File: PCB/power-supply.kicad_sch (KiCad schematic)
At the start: 18 parts, among them J2 DF63-5P-3.96DSA

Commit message: preliminary routing completed
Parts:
- removed DBG1, DBG2, DBG3, DBG4, DBG5, DBG6: ~, Oro Footprints:DebugPin, symbol Oro:DebugPin
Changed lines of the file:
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@@
   (junction (at 187.96 98.425) (diameter 0) (color 0 0 0 0)
-  )
-  (junction (at 195.58 100.965) (diameter 0) (color 0 0 0 0)
-  )
-  (junction (at 264.16 98.425) (diameter 0) (color 0 0 0 0)
   )
   (junction (at 218.44 118.745) (diameter 0) (color 0 0 0 0)
@@
     (property "Netclass" "5V" (at 144.145 92.71 0)
       (effects (font (size 1.27 1.27) italic) (justify left))
-    )
-  )
-  (symbol (lib_id "Oro:DebugPin") (at 59.055 100.33 180) (unit 1)
-    (in_bom no) (on_board yes) (dnp no)
-    (property "Reference" "DBG2" (at 53.34 100.33 0)
-      (effects (font (size 1.27 1.27)) hide)
-    )
-    (property "Value" "~" (at 59.055 100.33 0)
-      (effects (font (size 1.27 1.27)) hide)
-    )
-    (property "Footprint" "Oro Footprints:DebugPin" (at 57.785 102.87 0)
-      (effects (font (size 1.27 1.27)) hide)
-    )
-    (property "Datasheet" "" (at 59.055 100.33 0)
-      (effects (font (size 1.27 1.27)) hide)
-    )
-    (property "Sim.Enable" "0" (at 45.085 102.87 0)
-      (effects (font (size 1.27 1.27)) hide)
-    )
-    (pin "1")
-    (instances
-      (project "OroLink"
-        (path "/e89dcd22-1250-4a5b-b778-1c95a0dd623d/f955395e-bf1a-4ef3-9cfe-ec9d49f66988"
-          (reference "DBG2") (unit 1)
-        )
-      )
     )
   )
@@
     )
   )
-  (symbol (lib_id "Oro:DebugPin") (at 59.055 102.87 180) (unit 1)
-    (in_bom no) (on_board yes) (dnp no)
-    (property "Reference" "DBG3" (at 53.34 102.87 0)
-      (effects (font (size 1.27 1.27)) hide)
-    )
-    (property "Value" "~" (at 59.055 102.87 0)
-      (effects (font (size 1.27 1.27)) hide)
-    )
-    (property "Footprint" "Oro Footprints:DebugPin" (at 57.785 105.41 0)
-      (effects (font (size 1.27 1.27)) hide)
-    )
-    (property "Datasheet" "" (at 59.055 102.87 0)
-      (effects (font (size 1.27 1.27)) hide)
-    )
-    (property "Sim.Enable" "0" (at 45.085 105.41 0)
-      (effects (font (size 1.27 1.27)) hide)
-    )
-    (pin "1")
-    (instances
-      (project "OroLink"
-        (path "/e89dcd22-1250-4a5b-b778-1c95a0dd623d/f955395e-bf1a-4ef3-9cfe-ec9d49f66988"
-          (reference "DBG3") (unit 1)
-        )
-      )
-    )
-  )
   (symbol (lib_id "SamacSys_Parts:CSD13380F3T") (at 125.095 112.395 90) (mirror x) (unit 1)
     (in_bom yes) (on_board yes) (dnp no) (fields_autoplaced)
@@
         (path "/e89dcd22-1250-4a5b-b778-1c95a0dd623d/f955395e-bf1a-4ef3-9cfe-ec9d49f66988"
           (reference "R8") (unit 1)
-        )
-      )
-    )
-  )
-  (symbol (lib_id "Oro:DebugPin") (at 264.16 98.425 0) (unit 1)
-    (in_bom no) (on_board yes) (dnp no)
-    (property "Reference" "DBG6" (at 269.875 98.425 0)
-      (effects (font (size 1.27 1.27)) hide)
-    )
-    (property "Value" "~" (at 264.16 98.425 0)
-      (effects (font (size 1.27 1.27)) hide)
-    )
-    (property "Footprint" "Oro Footprints:DebugPin" (at 265.43 95.885 0)
-      (effects (font (size 1.27 1.27)) hide)
-    )
-    (property "Datasheet" "" (at 264.16 98.425 0)
-      (effects (font (size 1.27 1.27)) hide)
-    )
-    (property "Sim.Enable" "0" (at 278.13 95.885 0)
-      (effects (font (size 1.27 1.27)) hide)
-    )
-    (pin "1")
-    (instances
-      (project "OroLink"
-        (path "/e89dcd22-1250-4a5b-b778-1c95a0dd623d/f955395e-bf1a-4ef3-9cfe-ec9d49f66988"
-          (reference "DBG6") (unit 1)
         )
       )
@@
     )
   )
-  (symbol (lib_id "Oro:DebugPin") (at 59.055 105.41 180) (unit 1)
-    (in_bom no) (on_board yes) (dnp no)
-    (property "Reference" "DBG4" (at 53.34 105.41 0)
-      (effects (font (size 1.27 1.27)) hide)
-    )
-    (property "Value" "~" (at 59.055 105.41 0)
-      (effects (font (size 1.27 1.27)) hide)
-    )
-    (property "Footprint" "Oro Footprints:DebugPin" (at 57.785 107.95 0)
-      (effects (font (size 1.27 1.27)) hide)
-    )
-    (property "Datasheet" "" (at 59.055 105.41 0)
-      (effects (font (size 1.27 1.27)) hide)
-    )
-    (property "Sim.Enable" "0" (at 45.085 107.95 0)
-      (effects (font (size 1.27 1.27)) hide)
-    )
-    (pin "1")
-    (instances
-      (project "OroLink"
-        (path "/e89dcd22-1250-4a5b-b778-1c95a0dd623d/f955395e-bf1a-4ef3-9cfe-ec9d49f66988"
-          (reference "DBG4") (unit 1)
-        )
-      )
-    )
-  )
   (symbol (lib_id "Oro:BOM Part") (at 53.34 120.015 0) (unit 1)
     (in_bom yes) (on_board no) (dnp no)
@@
         )
       )
-    )
-  )
-  (symbol (lib_id "Oro:DebugPin") (at 195.58 100.965 180) (unit 1)
-    (in_bom no) (on_board yes) (dnp no)
-    (property "Reference" "DBG5" (at 189.865 100.965 0)
-      (effects (font (size 1.27 1.27)) hide)
-    )
-    (property "Value" "~" (at 195.58 100.965 0)
-      (effects (font (size 1.27 1.27)) hide)
-    )
-    (property "Footprint" "Oro Footprints:DebugPin" (at 194.31 103.505 0)
-      (effects (font (size 1.27 1.27)) hide)
-    )
-    (property "Datasheet" "" (at 195.58 100.965 0)
-      (effects (font (size 1.27 1.27)) hide)
-    )
-    (property "Sim.Enable" "0" (at 181.61 103.505 0)
-      (effects (font (size 1.27 1.27)) hide)
-    )
-    (pin "1")
-    (instances
-      (project "OroLink"
-        (path "/e89dcd22-1250-4a5b-b778-1c95a0dd623d/f955395e-bf1a-4ef3-9cfe-ec9d49f66988"
-          (reference "DBG5") (unit 1)
-        )
-      )
-    )
-  )
-  (symbol (lib_id "Oro:DebugPin") (at 59.055 97.79 180) (unit 1)
-    (in_bom no) (on_board yes) (dnp no)
-    (property "Reference" "DBG1" (at 53.34 97.79 0)
-      (effects (font (size 1.27 1.27)) hide)
-    )
-    (property "Value" "~" (at 59.055 97.79 0)
-      (effects (font (size 1.27 1.27)) hide)
-    )
-    (property "Footprint" "Oro Footprints:DebugPin" (at 57.785 100.33 0)
-      (effects (font (size 1.27 1.27)) hide)
-    )
-    (property "Datasheet" "" (at 59.055 97.79 0)
-      (effects (font (size 1.27 1.27)) hide)
-    )
-    (property "Sim.Enable" "0" (at 45.085 100.33 0)
-      (effects (font (size 1.27 1.27)) hide)
-    )
-    (pin "1")
-    (instances
-      (project "OroLink"
-        (path "/e89dcd22-1250-4a5b-b778-1c95a0dd623d/f955395e-bf1a-4ef3-9cfe-ec9d49f66988"
-          (reference "DBG1") (unit 1)
-        )
-      )

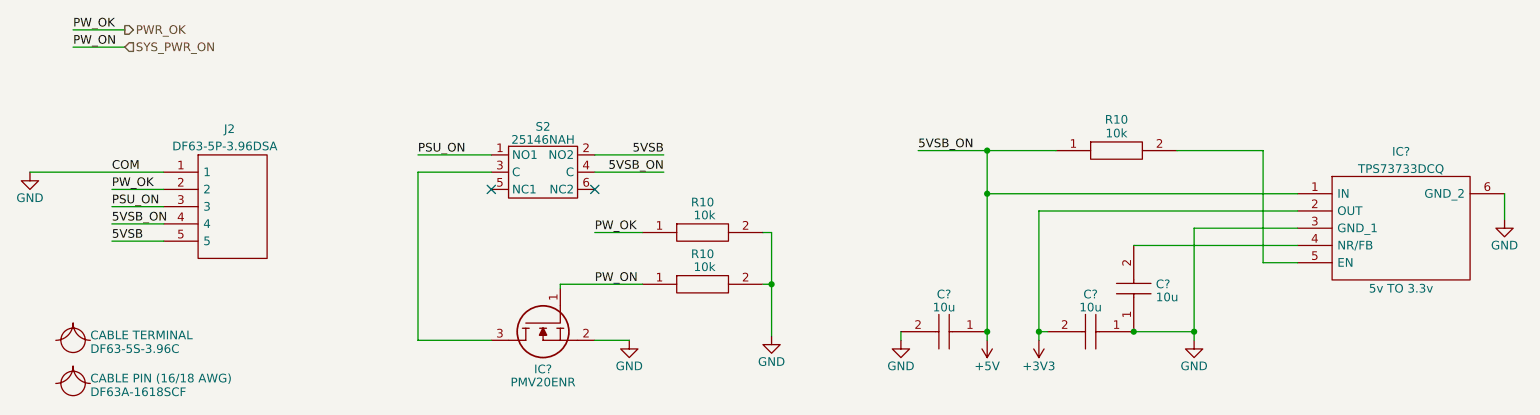
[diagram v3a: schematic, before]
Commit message: eliminate power switch in lieu of direct power + sys s.b. mosfet (closes #38)
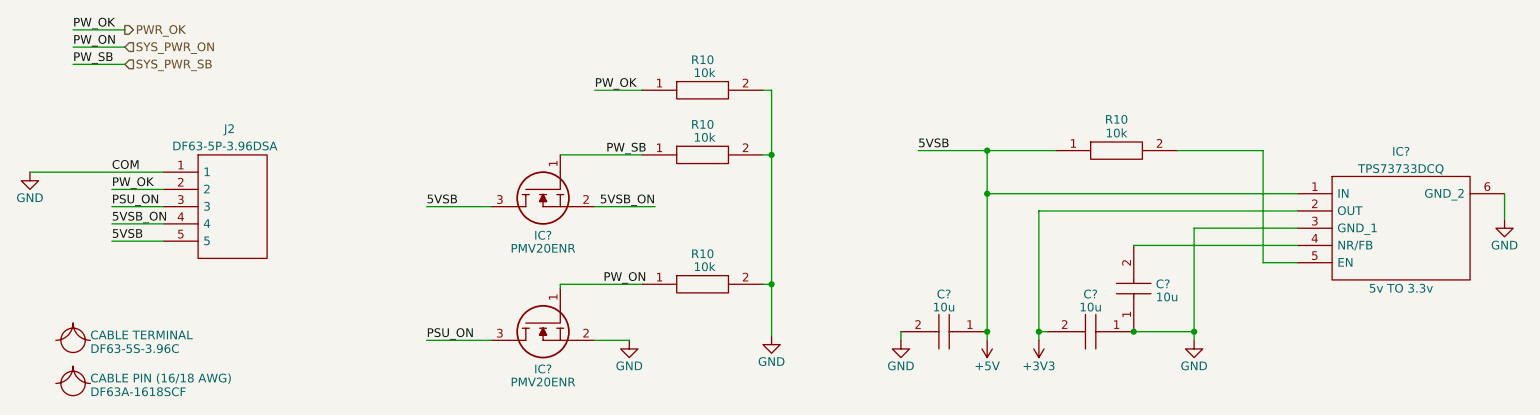
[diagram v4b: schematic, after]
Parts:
- removed S2: 25146NAH, Oro Footprints:25146NAH, symbol Oro:25146NAH
- added IC?: PMV20ENR, SamacSys_Parts:SOT95P230X110-3N, symbol SamacSys_Parts:CSD13380F3T
- added R10: 10k, RESC1005X40N, symbol SamacSys_Parts:RK73H1ETTP1002F
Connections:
- net 5VSB is gone; now on net +5V: J2.5
- net +5V: now also IC?.3; no longer J2.4
- net GND: now also R10.2
- net PSU_ON: now also IC?.3
- new net: IC?.1, R10.1
- new net 5VSB_ON: IC?.2, J2.4
- no-connect marks 2 -> 0
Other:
- moved on the sheet: R10

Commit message: switch out linear regular for one with larger max current (closes #43)
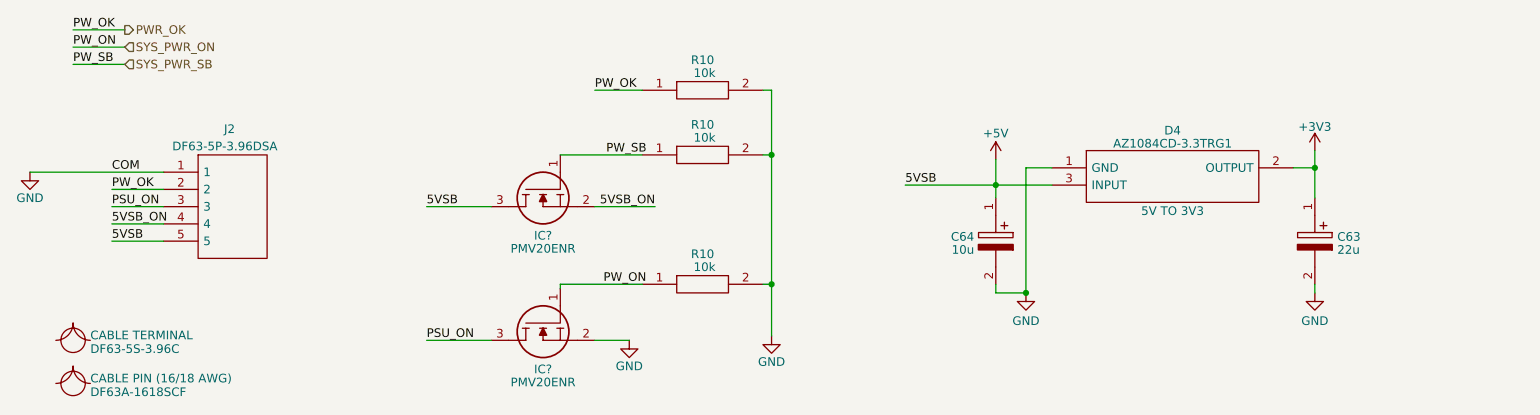
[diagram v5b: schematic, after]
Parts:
- removed C? (x3): 10u, SamacSys_Parts:CAPC2012X135N, symbol SamacSys_Parts:LMK212ABJ106KG8T
- removed IC?: TPS73733DCQ, SamacSys_Parts:SOT127P706X180-6N, symbol SamacSys_Parts:TPS73733DCQR
- removed R10: 10k, RESC1005X40N, symbol SamacSys_Parts:RK73H1ETTP1002F
- added C63: 22u, CAPAE660X800N, symbol SamacSys_Parts:UCZ1H220MCL1GS
- added C64: 10u, CAPAE430X610N, symbol SamacSys_Parts:VZT100M1HTR-0406
- added D4: AZ1084CD-3.3TRG1, AZ1084CD33TRG1, symbol SamacSys_Parts:AZ1084CD-3.3TRG1
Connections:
- net +3V3: now also C63.1, D4.2 (OUTPUT)
- net +5V: now also C64.1, D4.3 (INPUT)
- net GND: now also C63.2, C64.2, D4.1 (GND)

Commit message: initial rev6
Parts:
- renumbered C64 to C18, C63 to C19, D4 to D3
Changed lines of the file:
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@@
   (title_block
     (title "Oro Link")
-    (date "2023-06-02")
-    (rev "5")
+    (date "2023-07-02")
+    (rev "6")
     (company "Oro Operating System")
     (comment 1 "://oro.sh")
@@
   (symbol (lib_id "power:GND") (at 236.22 113.03 0) (unit 1)
     (in_bom yes) (on_board yes) (dnp no) (fields_autoplaced)
-    (property "Reference" "#PWR093" (at 236.22 119.38 0)
+    (property "Reference" "#PWR025" (at 236.22 119.38 0)
       (effects (font (size 1.27 1.27)) hide)
     )
@@
       (project "OroLink"
         (path "/e89dcd22-1250-4a5b-b778-1c95a0dd623d/f955395e-bf1a-4ef3-9cfe-ec9d49f66988"
-          (reference "#PWR093") (unit 1)
+          (reference "#PWR025") (unit 1)
         )
       )
@@
   (symbol (lib_id "SamacSys_Parts:AZ1084CD-3.3TRG1") (at 197.485 94.615 0) (unit 1)
     (in_bom yes) (on_board yes) (dnp no)
-    (property "Reference" "D4" (at 215.265 89.1159 0)
+    (property "Reference" "D3" (at 215.265 89.1159 0)
       (effects (font (size 1.27 1.27)))
     )
@@
       (project "OroLink"
         (path "/e89dcd22-1250-4a5b-b778-1c95a0dd623d/f955395e-bf1a-4ef3-9cfe-ec9d49f66988"
-          (reference "D4") (unit 1)
+          (reference "D3") (unit 1)
         )
       )
@@
   (symbol (lib_id "SamacSys_Parts:UCZ1H220MCL1GS") (at 236.22 99.06 270) (unit 1)
     (in_bom yes) (on_board yes) (dnp no) (fields_autoplaced)
-    (property "Reference" "C63" (at 239.522 104.7663 90)
+    (property "Reference" "C19" (at 239.522 104.7663 90)
       (effects (font (size 1.27 1.27)) (justify left))
     )
@@
       (project "OroLink"
         (path "/e89dcd22-1250-4a5b-b778-1c95a0dd623d/f955395e-bf1a-4ef3-9cfe-ec9d49f66988"
-          (reference "C63") (unit 1)
+          (reference "C19") (unit 1)
         )
       )
@@
   (symbol (lib_id "power:GND") (at 193.675 113.03 0) (unit 1)
     (in_bom yes) (on_board yes) (dnp no) (fields_autoplaced)
-    (property "Reference" "#PWR091" (at 193.675 119.38 0)
+    (property "Reference" "#PWR023" (at 193.675 119.38 0)
       (effects (font (size 1.27 1.27)) hide)
     )
@@
       (project "OroLink"
         (path "/e89dcd22-1250-4a5b-b778-1c95a0dd623d/f955395e-bf1a-4ef3-9cfe-ec9d49f66988"
-          (reference "#PWR091") (unit 1)
+          (reference "#PWR023") (unit 1)
         )
       )
@@
   (symbol (lib_id "power:+3V3") (at 236.22 92.075 0) (unit 1)
     (in_bom yes) (on_board yes) (dnp no) (fields_autoplaced)
-    (property "Reference" "#PWR092" (at 236.22 95.885 0)
+    (property "Reference" "#PWR024" (at 236.22 95.885 0)
       (effects (font (size 1.27 1.27)) hide)
     )
@@
       (project "OroLink"
         (path "/e89dcd22-1250-4a5b-b778-1c95a0dd623d/f955395e-bf1a-4ef3-9cfe-ec9d49f66988"
-          (reference "#PWR092") (unit 1)
+          (reference "#PWR024") (unit 1)
         )
       )
@@
   (symbol (lib_id "SamacSys_Parts:VZT100M1HTR-0406") (at 189.23 99.06 270) (unit 1)
     (in_bom yes) (on_board yes) (dnp no)
-    (property "Reference" "C64" (at 186.055 104.759 90)
+    (property "Reference" "C18" (at 186.055 104.759 90)
       (effects (font (size 1.27 1.27)) (justify right))
     )
@@
       (project "OroLink"
         (path "/e89dcd22-1250-4a5b-b778-1c95a0dd623d/f955395e-bf1a-4ef3-9cfe-ec9d49f66988"
-          (reference "C64") (unit 1)
+          (reference "C18") (unit 1)
         )
       )
@@
       (project "OroLink"
         (path "/e89dcd22-1250-4a5b-b778-1c95a0dd623d/f955395e-bf1a-4ef3-9cfe-ec9d49f66988"
-          (reference "#PWR094") (unit 1)
-        )
-      )
+          (reference "#PWR022") (unit 1)
+        )
+      )

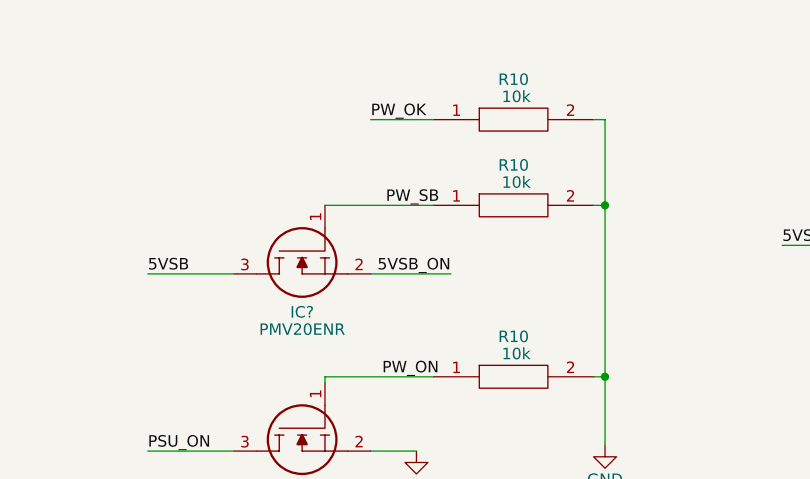
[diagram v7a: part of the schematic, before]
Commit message: add missing PSU standby enable line
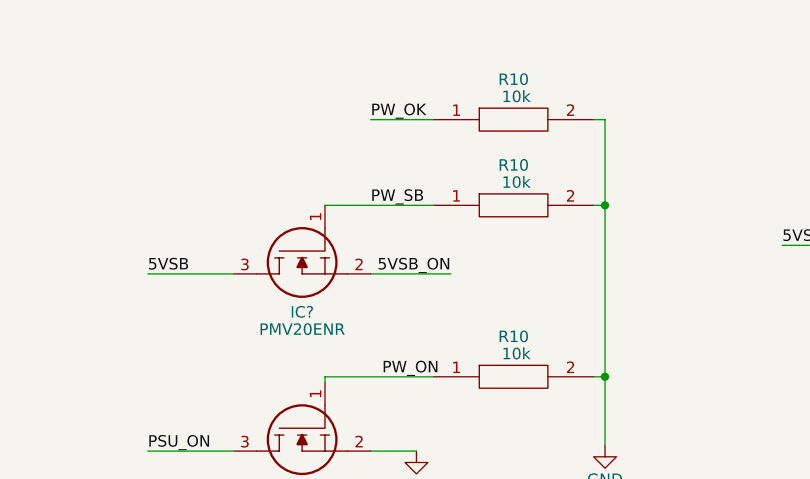
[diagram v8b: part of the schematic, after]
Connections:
- net SYS_PWR_SB: now also IC?.1, R10.1
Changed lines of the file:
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@@
     (effects (font (size 1.27 1.27)) (justify left bottom))
   )
-  (label "PW_SB" (at 137.795 92.71 180) (fields_autoplaced)
-    (effects (font (size 1.27 1.27)) (justify right bottom))
+  (label "PW_SB" (at 130.175 92.71 0) (fields_autoplaced)
+    (effects (font (size 1.27 1.27)) (justify left bottom))
   )
   (label "5VSB" (at 59.055 105.41 0) (fields_autoplaced)
